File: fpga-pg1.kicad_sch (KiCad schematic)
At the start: 38 parts, among them U6 XC7A15T-CSG325

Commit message: stuff
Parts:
- removed TP33, TP34, TP35, TP36, TP37, TP38, TP39, TP40, TP41, TP42, TP43, TP44, TP45, TP46, TP47, TP48: TestPoint_Small, symbol Connector:TestPoint_Small
- added TP49, TP50, TP51, TP52, TP53, TP54, TP55, TP56, TP57, TP58, TP59, TP60, TP61, TP62, TP63, TP64, TP65, TP66, TP67, TP68, TP69, TP70, TP71, TP72, TP73, TP74, TP75, TP76, TP77, TP78, TP79, TP80: TestPoint_Small, symbol Connector:TestPoint_Small
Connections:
- net DI.DI1+: now also TP49.1
- net DI.DI1-: now also TP50.1
- net DI.DI10+: now also TP67.1
- net DI.DI10-: now also TP68.1
- net DI.DI11+: now also TP69.1
- net DI.DI11-: now also TP70.1
- net DI.DI12+: now also TP71.1
- net DI.DI12-: now also TP72.1
- net DI.DI13+: now also TP73.1
- net DI.DI13-: now also TP74.1
- net DI.DI14+: now also TP75.1
- net DI.DI14-: now also TP76.1
- net DI.DI15+: now also TP77.1
- net DI.DI15-: now also TP78.1
- net DI.DI16+: now also TP79.1
- net DI.DI16-: now also TP80.1
- net DI.DI2+: now also TP51.1
- net DI.DI2-: now also TP52.1
- net DI.DI3+: now also TP53.1
- net DI.DI3-: now also TP54.1
- net DI.DI4+: now also TP55.1
- net DI.DI4-: now also TP56.1
- net DI.DI5+: now also TP57.1
- net DI.DI5-: now also TP58.1
- net DI.DI6+: now also TP59.1
- net DI.DI6-: now also TP60.1
- net DI.DI7+: now also TP61.1
- net DI.DI7-: now also TP62.1
- net DI.DI8+: now also TP63.1
- net DI.DI8-: now also TP64.1
- net DI.DI9+: now also TP65.1
- net DI.DI9-: now also TP66.1
- net DO.DO10+: no longer names the net of U6.T14 (IO_L13P_T2_MRCC_14)
- net DO.DO10-: no longer names the net of U6.T15 (IO_L13N_T2_MRCC_14)
- net DO.DO11+: no longer names the net of U6.R16 (IO_L14P_T2_SRCC_14)
- net DO.DO11-: no longer names the net of U6.R17 (IO_L14N_T2_SRCC_14)
- net DO.DO12+: no longer names the net of U6.R18 (IO_L15P_T2_DQS_RDWR_B_14)
- net DO.DO12-: no longer names the net of U6.T18 (IO_L15N_T2_DQS_DOUT_CSO_B_14)
- net DO.DO13+: no longer names the net of U6.T17 (IO_L16P_T2_CSI_B_14)
- net DO.DO13-: no longer names the net of U6.U17 (IO_L16N_T2_A15_D31_14)
- net DO.DO14+: no longer names the net of U6.U15 (IO_L17P_T2_A14_D30_14)
- net DO.DO14-: no longer names the net of U6.U16 (IO_L17N_T2_A13_D29_14)
- net DO.DO15+: no longer names the net of U6.V16 (IO_L18P_T2_A12_D28_14)
- net DO.DO15-: no longer names the net of U6.V17 (IO_L18N_T2_A11_D27_14)
- net DO.DO16+: no longer names the net of U6.R13 (IO_L19P_T3_A10_D26_14)
- net DO.DO16-: no longer names the net of U6.T13 (IO_L19N_T3_A09_D25_VREF_14)
- net DO.DO9+: no longer names the net of U6.P14 (IO_L12P_T1_MRCC_14)
- net DO.DO9-: no longer names the net of U6.R15 (IO_L12N_T1_MRCC_14)

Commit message: changed ddr3 pinning according to hard-ip in vivado
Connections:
- net DI.DI1+: no longer U6.D8 (IO_L1P_T0_AD0P_15)
- net DI.DI1-: no longer U6.C8 (IO_L1N_T0_AD0N_15)
- net DI.DI10+: no longer U6.B14 (IO_L10P_T1_AD11P_15)
- net DI.DI10-: no longer U6.A15 (IO_L10N_T1_AD11N_15)
- net DI.DI11+: no longer U6.D13 (IO_L11P_T1_SRCC_15)
- net DI.DI11-: no longer U6.C13 (IO_L11N_T1_SRCC_15)
- net DI.DI12+: no longer U6.E13 (IO_L12P_T1_MRCC_15)
- net DI.DI12-: no longer U6.D14 (IO_L12N_T1_MRCC_15)
- net DI.DI13+: no longer U6.E15 (IO_L13P_T2_MRCC_15)
- net DI.DI13-: no longer U6.D15 (IO_L13N_T2_MRCC_15)
- net DI.DI14+: no longer U6.E16 (IO_L14P_T2_SRCC_15)
- net DI.DI14-: no longer U6.D16 (IO_L14N_T2_SRCC_15)
- net DI.DI15+: no longer U6.B16 (IO_L15P_T2_DQS_15)
- net DI.DI15-: no longer U6.A17 (IO_L15N_T2_DQS_ADV_B_15)
- net DI.DI16+: no longer U6.C16 (IO_L16P_T2_A28_15)
- net DI.DI16-: no longer U6.B17 (IO_L16N_T2_A27_15)
- net DI.DI2+: no longer U6.D9 (IO_L2P_T0_AD8P_15)
- net DI.DI2-: no longer U6.C9 (IO_L2N_T0_AD8N_15)
- net DI.DI3+: no longer U6.B9 (IO_L3P_T0_DQS_AD1P_15)
- net DI.DI3-: no longer U6.A9 (IO_L3N_T0_DQS_AD1N_15)
- net DI.DI4+: no longer U6.C11 (IO_L4P_T0_15)
- net DI.DI4-: no longer U6.B11 (IO_L4N_T0_15)
- net DI.DI5+: no longer U6.B10 (IO_L5P_T0_AD9P_15)
- net DI.DI5-: no longer U6.A10 (IO_L5N_T0_AD9N_15)
- net DI.DI6+: no longer U6.D11 (IO_L6P_T0_15)
- net DI.DI6-: no longer U6.C12 (IO_L6N_T0_VREF_15)
- net DI.DI7+: no longer U6.B12 (IO_L7P_T1_AD2P_15)
- net DI.DI7-: no longer U6.A12 (IO_L7N_T1_AD2N_15)
- net DI.DI8+: no longer U6.A13 (IO_L8P_T1_AD10P_15)
- net DI.DI8-: no longer U6.A14 (IO_L8N_T1_AD10N_15)
- net DI.DI9+: no longer U6.C14 (IO_L9P_T1_DQS_AD3P_15)
- net DI.DI9-: no longer U6.B15 (IO_L9N_T1_DQS_AD3N_15)
- net DO.DO1+: no longer U6.J18 (IO_L3P_T0_DQS_PUDC_B_14)
- net DO.DO1-: no longer U6.K18 (IO_L3N_T0_DQS_EMCCLK_14)
- net DO.DO2+: no longer U6.K17 (IO_L4P_T0_D04_14)
- net DO.DO2-: no longer U6.L18 (IO_L4N_T0_D05_14)
- net DO.DO3+: no longer U6.J14 (IO_L5P_T0_D06_14)
- net DO.DO3-: no longer U6.K15 (IO_L5N_T0_D07_14)
- net DO.DO4+: no longer U6.M16 (IO_L7P_T1_D09_14)
- net DO.DO4-: no longer U6.M17 (IO_L7N_T1_D10_14)
- net DO.DO5+: no longer U6.M14 (IO_L8P_T1_D11_14)
- net DO.DO5-: no longer U6.N14 (IO_L8N_T1_D12_14)
- net DO.DO6+: no longer U6.N16 (IO_L9P_T1_DQS_14)
- net DO.DO6-: no longer U6.N17 (IO_L9N_T1_DQS_D13_14)
- net DO.DO7+: no longer U6.N18 (IO_L10P_T1_D14_14)
- net DO.DO7-: no longer U6.P18 (IO_L10N_T1_D15_14)
- net DO.DO8+: no longer U6.P15 (IO_L11P_T1_SRCC_14)
- net DO.DO8-: no longer U6.P16 (IO_L11N_T1_SRCC_14)
- net DDR3_ADDR4: now reaches U6.P14 (IO_L12P_T1_MRCC_14)
- net DDR3_CLK_EN: now reaches U6.R13 (IO_L19P_T3_A10_D26_14)
- net DDR3_ADDR3: now reaches U6.R15 (IO_L12N_T1_MRCC_14)
- net DDR3_ADDR2: now reaches U6.R16 (IO_L14P_T2_SRCC_14)
- net DDR3_ADDR1: now reaches U6.R17 (IO_L14N_T2_SRCC_14)
- net DDR3_ADDR0: now reaches U6.R18 (IO_L15P_T2_DQS_RDWR_B_14)
- net DDR3_BLOCK_ADDR1: now reaches U6.T17 (IO_L16P_T2_CSI_B_14)
- net DDR3_BLOCK_ADDR2: now reaches U6.T18 (IO_L15N_T2_DQS_DOUT_CSO_B_14)
- net DDR3_ODT: now reaches U6.U14 (IO_L20P_T3_A08_D24_14)
- net DDR3_RAS#: now reaches U6.U15 (IO_L17P_T2_A14_D30_14)
- net DDR3_CAS#: now reaches U6.U16 (IO_L17N_T2_A13_D29_14)
- net DDR3_BLOCK_ADDR0: now reaches U6.U17 (IO_L16N_T2_A15_D31_14)
- net DDR3_CLK+: now reaches U6.V12 (IO_L21P_T3_DQS_14)
- net DDR3_CLK-: now reaches U6.V13 (IO_L21N_T3_DQS_A06_D22_14)
- net DDR3_WE#: now reaches U6.V16 (IO_L18P_T2_A12_D28_14)
- net DDR3_CS#: now reaches U6.V17 (IO_L18N_T2_A11_D27_14)
- new net DDR3_ADDR10: U6.N16 (IO_L9P_T1_DQS_14)
- new net DDR3_ADDR11: U6.N14 (IO_L8N_T1_D12_14)
- new net DDR3_ADDR12: U6.M14 (IO_L8P_T1_D11_14)
- new net DDR3_ADDR13: U6.M17 (IO_L7N_T1_D10_14)
- new net DDR3_ADDR14: U6.M16 (IO_L7P_T1_D09_14)
- new net DDR3_ADDR5: U6.P16 (IO_L11N_T1_SRCC_14)
- new net DDR3_ADDR6: U6.P15 (IO_L11P_T1_SRCC_14)
- new net DDR3_ADDR7: U6.P18 (IO_L10N_T1_D15_14)
- new net DDR3_ADDR8: U6.N18 (IO_L10P_T1_D14_14)
- new net DDR3_ADDR9: U6.N17 (IO_L9N_T1_DQS_D13_14)
- new net DDR3_DQ0: U6.C8 (IO_L1N_T0_AD0N_15)
- new net DDR3_DQ1: U6.D9 (IO_L2P_T0_AD8P_15)
- new net DDR3_DQ10: U6.A14 (IO_L8N_T1_AD10N_15)
- new net DDR3_DQ11: U6.B14 (IO_L10P_T1_AD11P_15)
- new net DDR3_DQ12: U6.A15 (IO_L10N_T1_AD11N_15)
- new net DDR3_DQ13: U6.D13 (IO_L11P_T1_SRCC_15)
- new net DDR3_DQ14: U6.C13 (IO_L11N_T1_SRCC_15)
- new net DDR3_DQ15: U6.E13 (IO_L12P_T1_MRCC_15)
- new net DDR3_DQ2: U6.C9 (IO_L2N_T0_AD8N_15)
- new net DDR3_DQ3: U6.C11 (IO_L4P_T0_15)
- new net DDR3_DQ4: U6.B11 (IO_L4N_T0_15)
- new net DDR3_DQ5: U6.B10 (IO_L5P_T0_AD9P_15)
- new net DDR3_DQ6: U6.A10 (IO_L5N_T0_AD9N_15)
- new net DDR3_DQ7: U6.D11 (IO_L6P_T0_15)
- new net DDR3_DQ8: U6.A12 (IO_L7N_T1_AD2N_15)
- new net DDR3_DQ9: U6.A13 (IO_L8P_T1_AD10P_15)
- new net DDR3_LDM: U6.D8 (IO_L1P_T0_AD0P_15)
- new net DDR3_LDQS+: U6.B9 (IO_L3P_T0_DQS_AD1P_15)
- new net DDR3_LDQS-: U6.A9 (IO_L3N_T0_DQS_AD1N_15)
- new net DDR3_RESET#: U6.D14 (IO_L12N_T1_MRCC_15)
- new net DDR3_UDM: U6.B12 (IO_L7P_T1_AD2P_15)
- new net DDR3_UDQS+: U6.C14 (IO_L9P_T1_DQS_AD3P_15)
- new net DDR3_UDQS-: U6.B15 (IO_L9N_T1_DQS_AD3N_15)
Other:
- moved on the sheet: TP17, TP18, TP19, TP20, TP21, TP22, TP23, TP24, TP25, TP26, TP27, TP28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

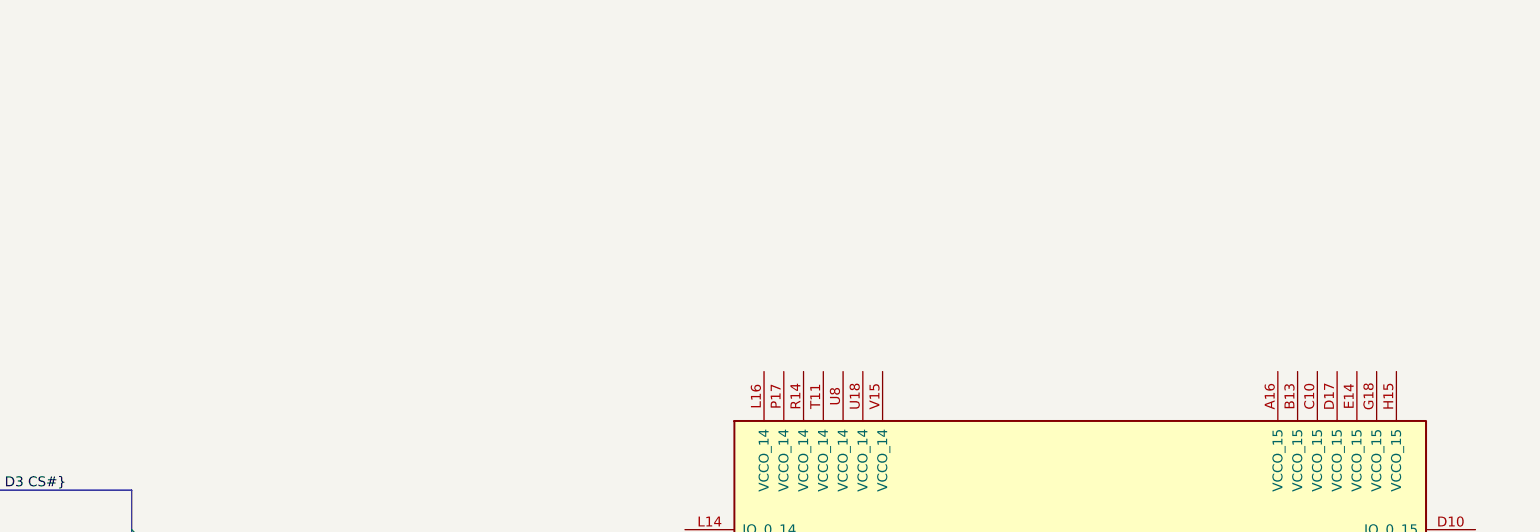
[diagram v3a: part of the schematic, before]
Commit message: did preliminary routing on ddr3, fixed clearance rule
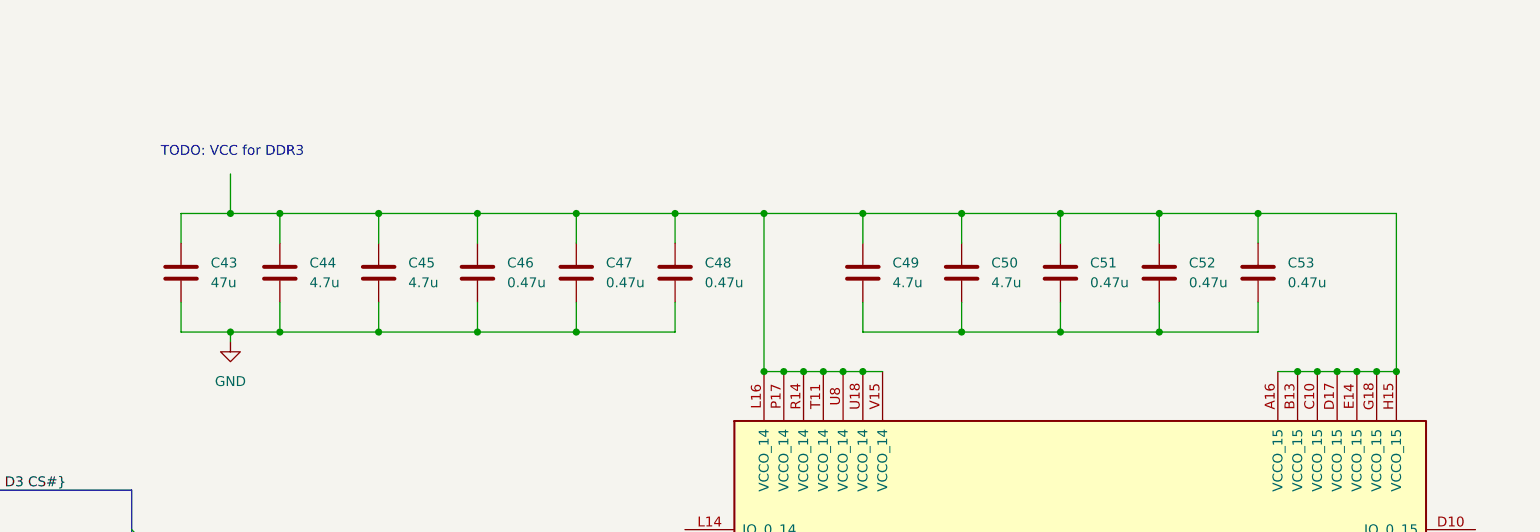
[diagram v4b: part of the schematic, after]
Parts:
- added C43: 47u, Capacitor_SMD:C_1210_3225Metric, symbol Device:C
- added C44, C45, C49, C50: 4.7u, Capacitor_SMD:C_0805_2012Metric, symbol Device:C
- added C46, C47, C48, C51, C52, C53: 0.47u, Capacitor_SMD:C_0603_1608Metric, symbol Device:C
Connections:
- net at U6.A16 (VCCO_15): now also U6.B13 (VCCO_15), U6.C10 (VCCO_15), U6.D17 (VCCO_15), U6.E14 (VCCO_15), U6.G18 (VCCO_15), U6.H15 (VCCO_15), U6.L16 (VCCO_14), U6.P17 (VCCO_14), U6.R14 (VCCO_14), U6.T11 (VCCO_14), U6.U18 (VCCO_14), U6.U8 (VCCO_14), U6.V15 (VCCO_14), C43.1, C44.1, C45.1, C46.1, C47.1, C48.1, C49.1, C50.1, C51.1, C52.1, C53.1
- new net: C49.2, C50.2, C51.2, C52.2, C53.2
- new net GND: C43.2, C44.2, C45.2, C46.2, C47.2, C48.2
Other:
- note added: "TODO: VCC for DDR3"

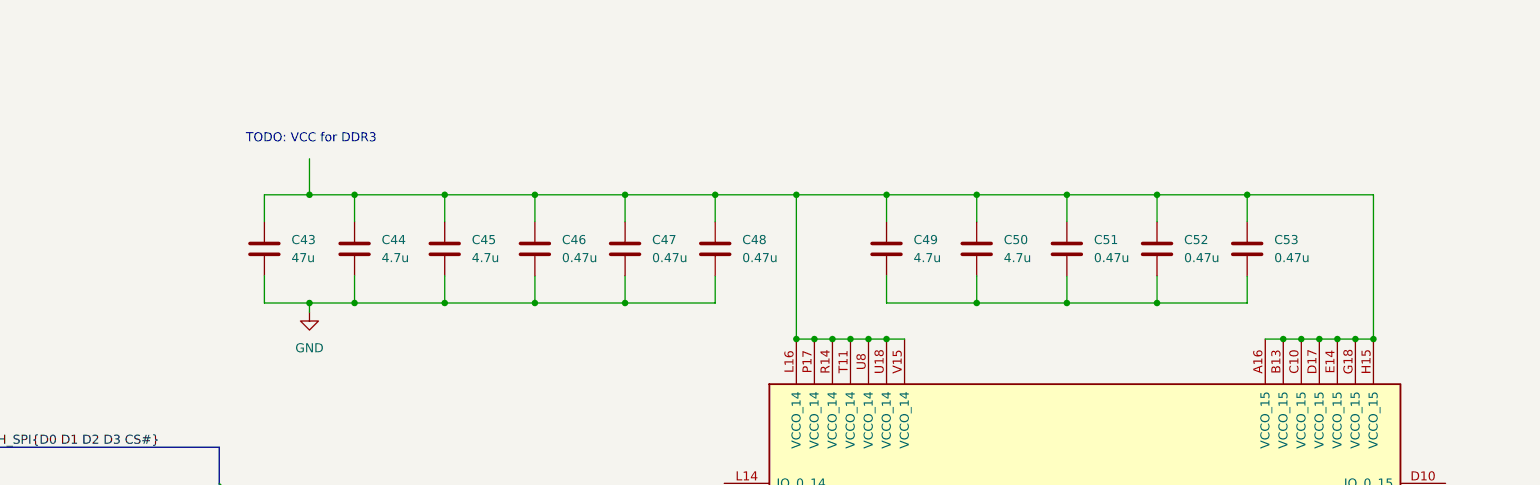
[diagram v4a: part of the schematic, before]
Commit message: placed decoupling caps for fpga
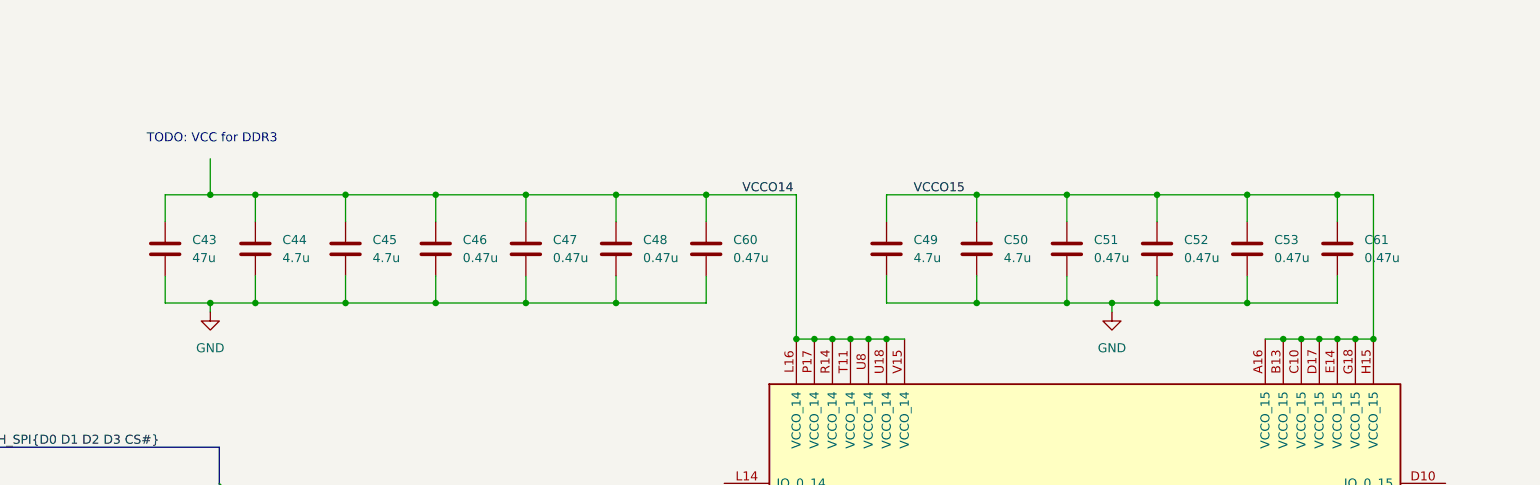
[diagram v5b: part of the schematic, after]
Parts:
- added C60, C61: 0.47u, Capacitor_SMD:C_0402_1005Metric, symbol Device:C
- C44, C45, C49, C50: footprint Capacitor_SMD:C_0805_2012Metric -> Capacitor_SMD:C_0402_1005Metric
- C46, C47, C48, C51, C52, C53: footprint Capacitor_SMD:C_0603_1608Metric -> Capacitor_SMD:C_0402_1005Metric
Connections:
- net GND: now also C49.2, C50.2, C51.2, C52.2, C53.2, C60.2, C61.2
- net VCCO14: now reaches C43.1, C44.1, C45.1, C46.1, C47.1, C48.1, U6.L16 (VCCO_14), U6.P17 (VCCO_14), U6.R14 (VCCO_14), U6.T11 (VCCO_14), U6.U18 (VCCO_14), U6.U8 (VCCO_14), U6.V15 (VCCO_14)
- net VCCO14: now also C60.1; no longer C49.1, C50.1, C51.1, C52.1, C53.1, U6.A16 (VCCO_15), U6.B13 (VCCO_15), U6.C10 (VCCO_15), U6.D17 (VCCO_15), U6.E14 (VCCO_15), U6.G18 (VCCO_15), U6.H15 (VCCO_15)
- new net VCCO15: C49.1, C50.1, C51.1, C52.1, C53.1, C61.1, U6.A16 (VCCO_15), U6.B13 (VCCO_15), U6.C10 (VCCO_15), U6.D17 (VCCO_15), U6.E14 (VCCO_15), U6.G18 (VCCO_15), U6.H15 (VCCO_15)
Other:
- moved on the sheet: C43, C44, C45, C46, C47, C48

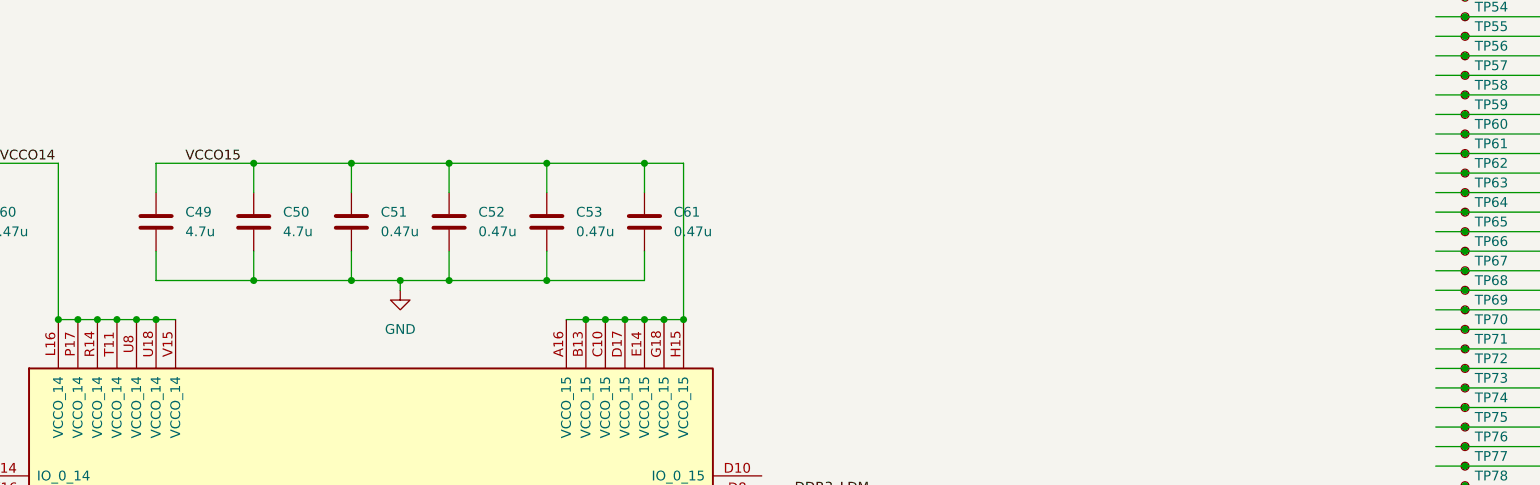
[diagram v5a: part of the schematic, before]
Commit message: more power-work, vccint needs to be moved to left side still
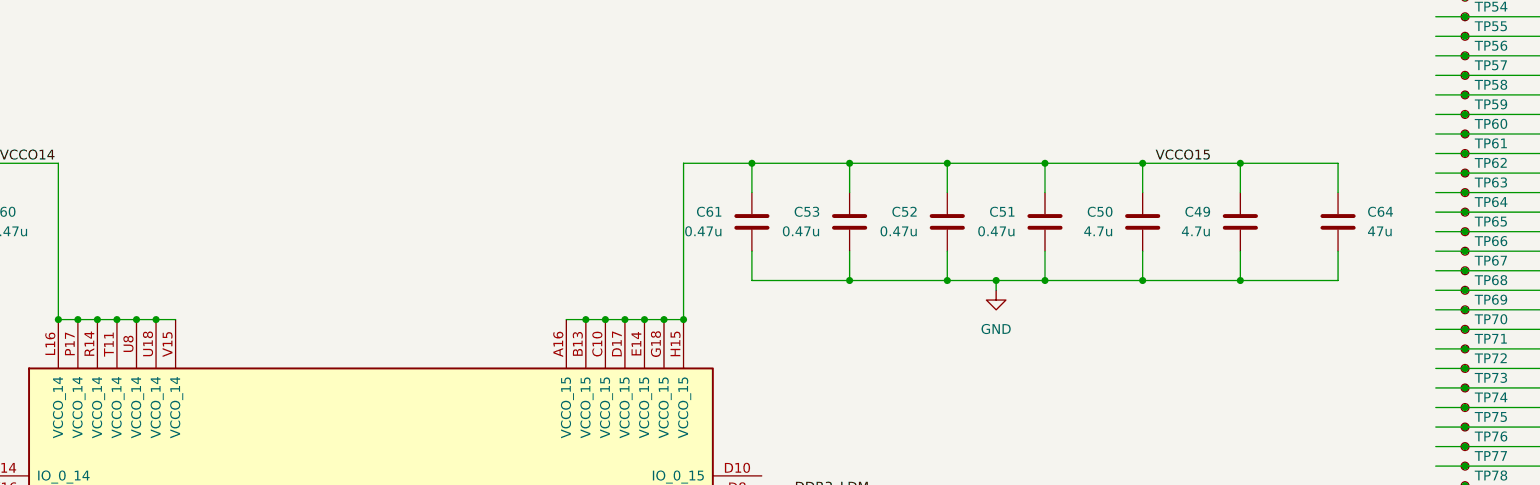
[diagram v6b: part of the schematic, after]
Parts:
- added C64: 47u, Capacitor_SMD:C_1210_3225Metric, symbol Device:C
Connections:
- net GND: now also C64.2
- net VCCO15: now also C64.1
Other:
- moved on the sheet: C49, C50, C51, C52, C53, C61

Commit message: started changing package, added correct decoupling
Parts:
- removed U6: XC7A15T-CSG325, Package_BGA:Xilinx_CSG325, symbol FPGA_Xilinx_Artix7:XC7A15T-CSG325
- added U1: XC7A35T-FGG484, Package_BGA:Xilinx_FGG484, symbol FPGA_Xilinx_Artix7:XC7A35T-FGG484
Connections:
- net VCCO15 is gone; now on net VCCO14: C49.1, C50.1, C51.1, C52.1, C53.1, C61.1, C64.1
- net VCCO14: now also U1.M14 (VCCO_14), U1.P18 (VCCO_14), U1.R15 (VCCO_14), U1.T22 (VCCO_14), U1.U19 (VCCO_14), U1.Y20 (VCCO_14); no longer C43.1, C44.1, C45.1, C46.1, C47.1, C48.1, C60.1
- new net VCCO13: C43.1, C44.1, C45.1, C46.1, C47.1, C48.1, C60.1, U1.AA17 (VCCO_13), U1.AB14 (VCCO_13), U1.V16 (VCCO_13), U1.W13 (VCCO_13), U1.Y10 (VCCO_13)
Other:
- moved on the sheet: C43, C44, C45, C46, C47, C48, C49, C50, C51, C52, C53, C60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

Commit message: connected almost all ddr3 pins, started placing decoupling caps
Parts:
- removed R11, R12, R13, R14, R15: 0, Resistor_SMD:R_0402_1005Metric_Pad0.72x0.64mm_HandSolder, symbol Device:R
